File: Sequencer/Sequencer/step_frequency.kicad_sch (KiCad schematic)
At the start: 4 parts

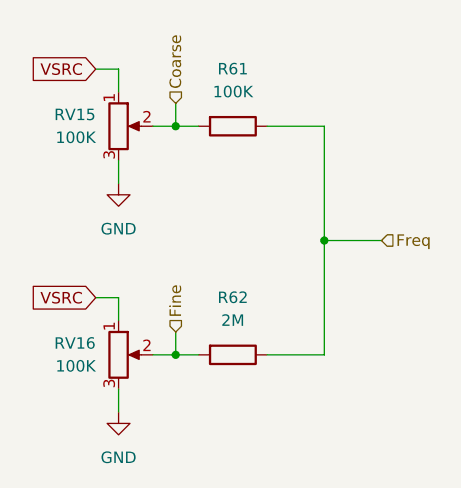
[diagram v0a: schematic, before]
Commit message: Sequencer - minor progress on routing
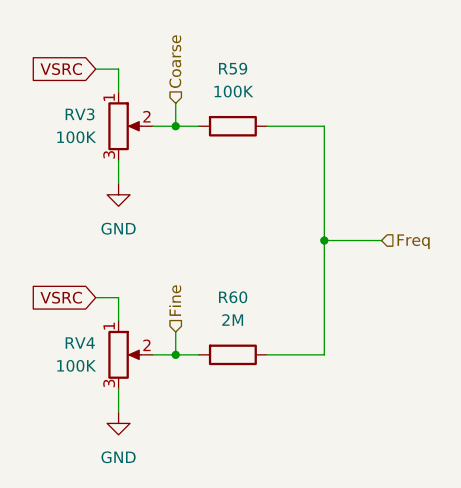
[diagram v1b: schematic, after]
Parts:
- R59: renamed from R61; footprint Resistor_THT:R_Axial_DIN0207_L6.3mm_D2.5mm_P7.62mm_Horizontal -> Library:R_Axial_DIN0207_L6.3mm_D2.5mm_P7.62mm_Horizontal
- R60: renamed from R62; footprint Resistor_THT:R_Axial_DIN0207_L6.3mm_D2.5mm_P7.62mm_Horizontal -> Library:R_Axial_DIN0207_L6.3mm_D2.5mm_P7.62mm_Horizontal
- renumbered RV15 to RV3, RV16 to RV4

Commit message: Sequencer - mostly positionned
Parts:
- renumbered R59 to R49, R60 to R50

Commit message: Sequencer - misc
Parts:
- renumbered R49 to R59, R50 to R60
